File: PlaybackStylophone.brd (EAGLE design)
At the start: 111.8 x 76.2 mm, 53 parts, among them SW6 ON/OFF

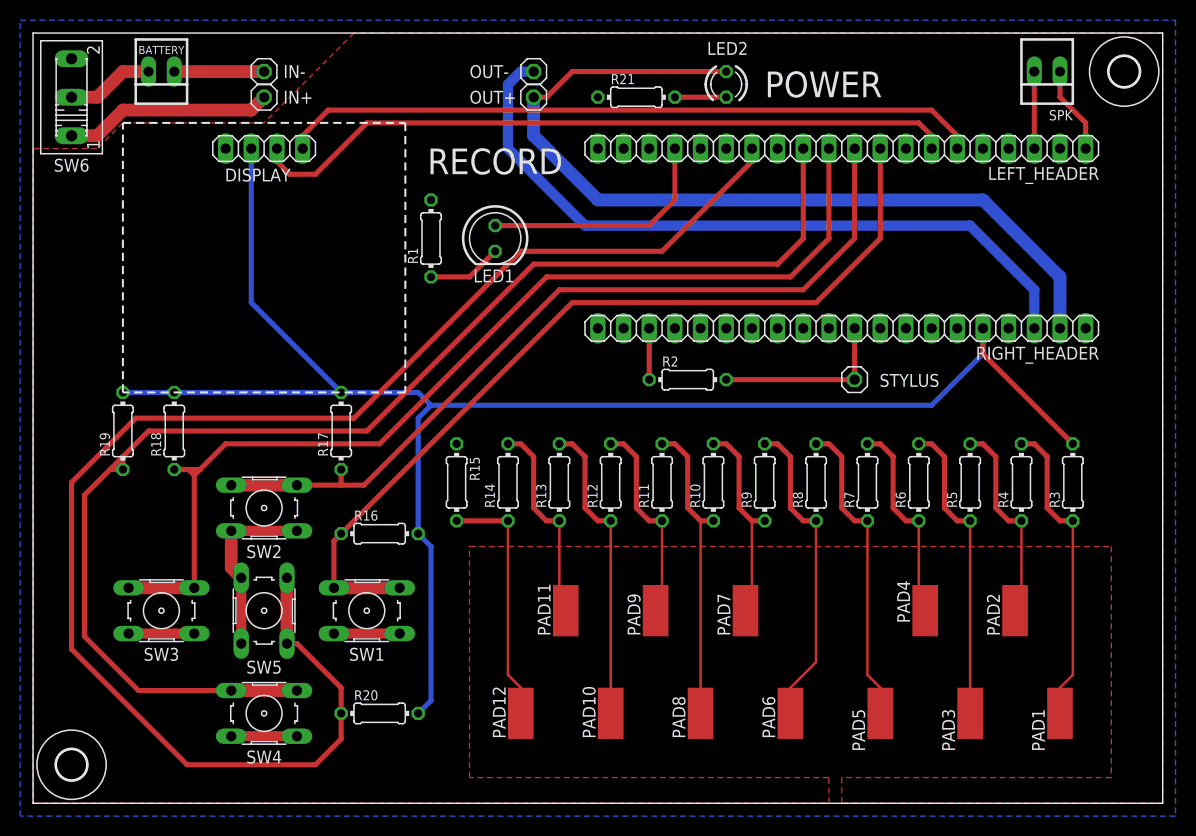
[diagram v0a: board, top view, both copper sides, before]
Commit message: Optimized routes layout on pcb
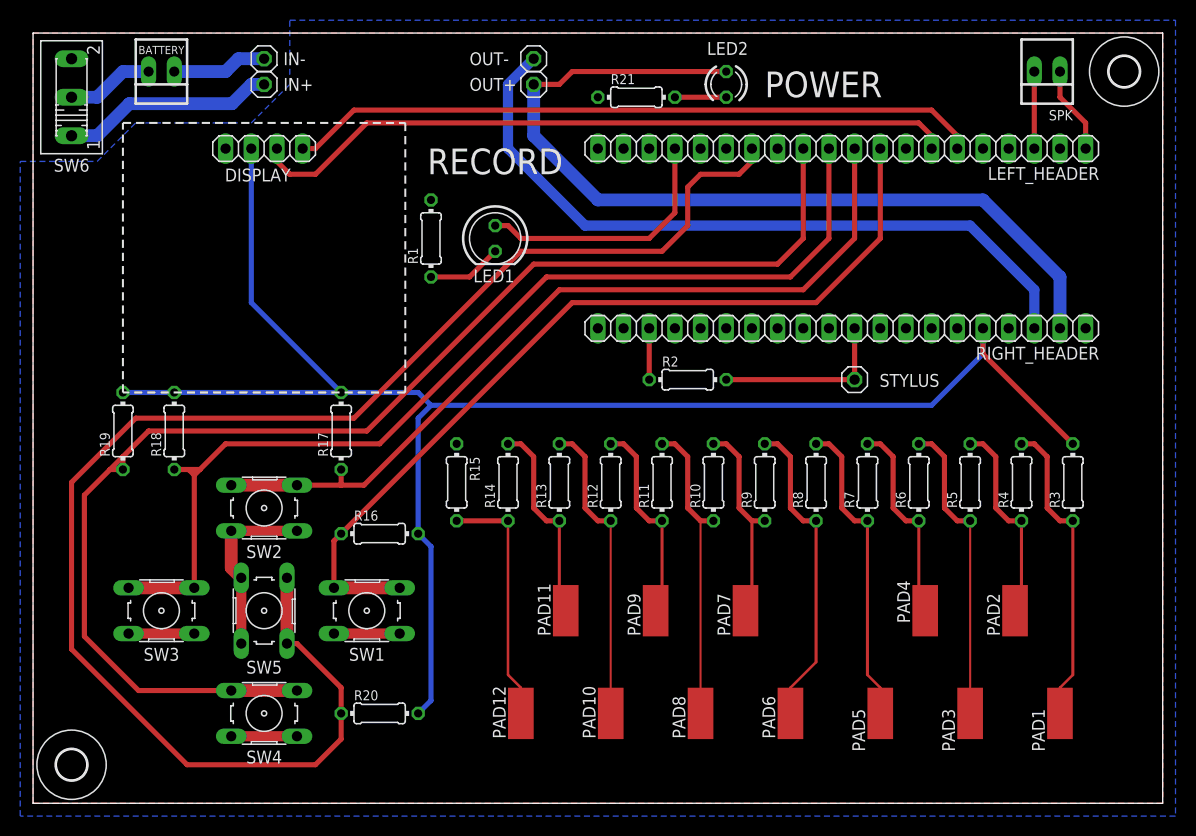
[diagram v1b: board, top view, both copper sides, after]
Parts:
- moved IN+ 1.27 mm to (22.9, 71.1)
- moved OUT+ 1.27 mm to (49.5, 71.1)
- moved IN- 1.27 mm to (22.9, 73.7)
- moved OUT- 1.27 mm to (49.5, 73.7)
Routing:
- net GP10: track 149.4 -> 151.7 mm
- net GP13: track 23.9 -> 25.7 mm
- net VSYS: track 86.8 -> 87.6 mm
- net SDA/GP4: track 69.4 -> 68.7 mm
- net B-SW: track 20.6 -> 21.2 mm
- net GND: track 121.4 -> 121.9 mm
- net B-GND: track 8.89 -> 9.42 mm

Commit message: Added low-pass filter
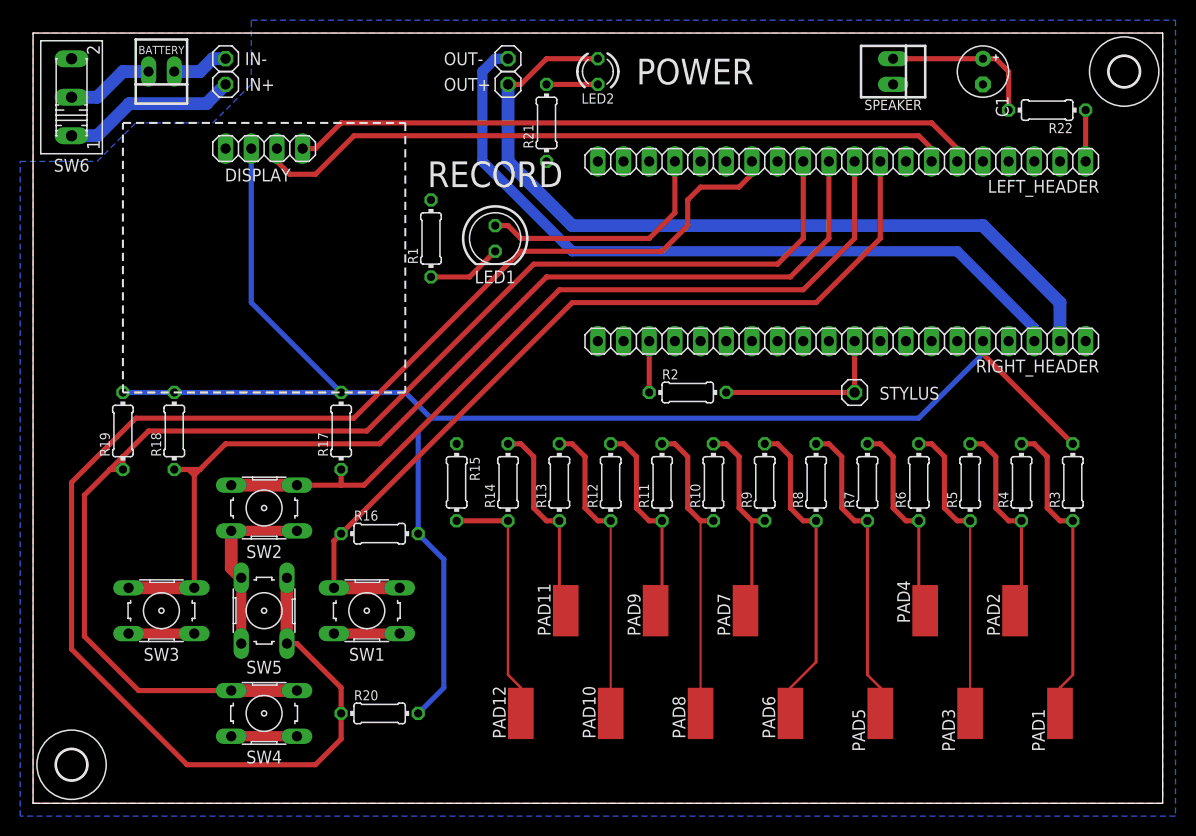
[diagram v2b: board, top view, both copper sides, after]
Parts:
- removed SPK: SPEAKER, con-molex:22-23-2021
- added C1: 10u, rcl:E2,5-5
- added R22: 10, rcl:0204/7
- added SPEAKER: SPEAKER, con-molex:22-23-2021
- moved LED2 12.8 mm to (55.9, 72.4)
- moved R21 9.25 mm to (50.8, 67.3), turned to 90 degrees
- moved IN+ 3.81 mm to (19.1, 71.1)
- moved IN- 3.81 mm to (19.1, 73.7)
- moved OUT+ 2.54 mm to (47.0, 71.1)
- moved OUT- 2.54 mm to (47.0, 73.7)
- moved RIGHT_HEADER 1.27 mm to (80.0, 45.7)
- moved LEFT_HEADER 1.27 mm to (80.0, 63.5)
- moved R2 1.27 mm to (64.8, 40.6)
- moved STYLUS 1.27 mm to (81.3, 40.6)
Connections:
- new net N$1: C1.+, R22.2, SPEAKER.1
- net GND: now also C1.-, SPEAKER.2; no longer SPK.2
- net TX/GP0: now also R22.1; no longer SPK.1
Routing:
- net N$1: track 0.00 -> 15.8 mm
- net VSYS: track 87.6 -> 81.8 mm
- net GND: track 121.9 -> 117.3 mm
- net B-GND: track 9.42 -> 5.61 mm
- net B-SW: track 21.2 -> 17.3 mm
- net TX/GP0: track 8.67 -> 5.08 mm
- net +3V3: track 165.2 -> 163.5 mm
- net GP9: track 130.3 -> 129.0 mm
- net GP8: track 103.8 -> 102.5 mm
- net GP13: track 25.7 -> 24.4 mm
- net GP7: track 82.2 -> 81.0 mm
- net GP6: track 86.5 -> 85.2 mm
- net GP10: track 151.7 -> 150.4 mm
- net SDA/GP4: track 68.7 -> 68.1 mm
- net SCL/GP5: track 70.5 -> 69.9 mm
